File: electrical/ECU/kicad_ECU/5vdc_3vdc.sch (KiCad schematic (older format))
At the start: 8 parts

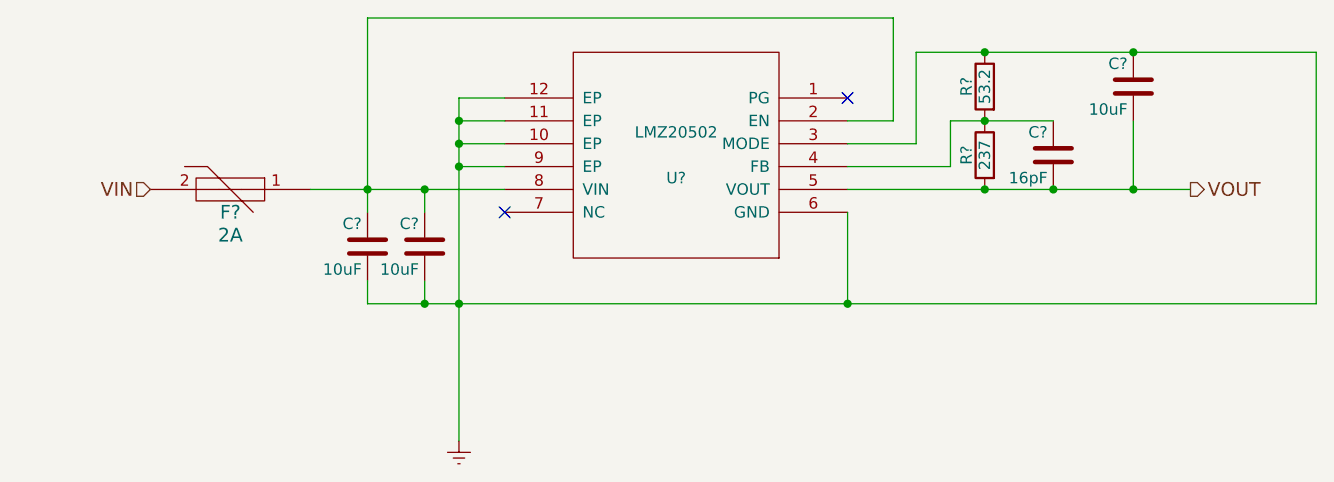
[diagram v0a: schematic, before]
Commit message: fixed some naming errors and initial round of double checking
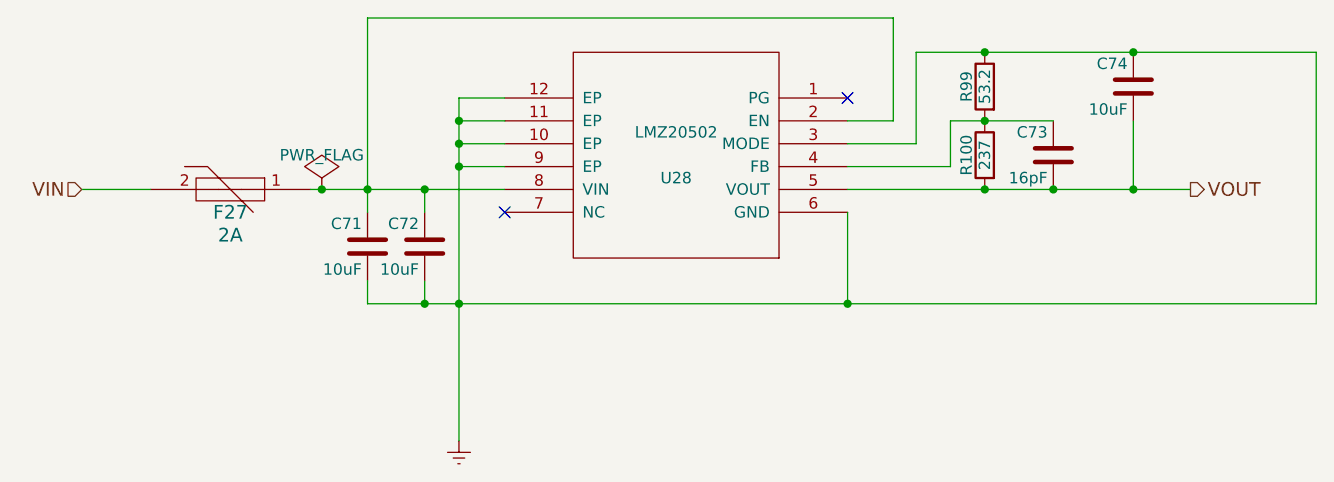
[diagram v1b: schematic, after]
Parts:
- gave numbers to parts that had none: 8
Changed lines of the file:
@@
 $Descr A4 11693 8268
 encoding utf-8
-Sheet 6 33
+Sheet 30 33
 Title "LMZ20502 5v to 3.3v"
 Date ""
@@
 $EndDescr
 $Comp
-L LMZ20502 U?
+L LMZ20502 U8
 U 1 1 59718A46
 P 5350 3350
-AR Path="/5978A36B/5978B8AA/59718A46" Ref="U?"  Part="1"
-AR Path="/597003E2/597189AE/59718A46" Ref="U?"  Part="1"
-F 0 "U?" H 5350 3250 50  0000 C CNN
+AR Path="/597003E2/597189AE/59718A46" Ref="U8"  Part="1"
+AR Path="/5978A36B/5978B8AA/59718A46" Ref="U28"  Part="1"
+F 0 "U28" H 5350 3250 50  0000 C CNN
 F 1 "LMZ20502" H 5350 3450 50  0000 C CNN
 F 2 "MODULE" H 5350 3350 50  0001 C CNN
@@
 	-1   0    0    -1
 $EndComp
-Text HLabel 3050 3500 0    60   Input ~ 0
+Text HLabel 2750 3500 0    60   Input ~ 0
 VIN
 NoConn ~ 4600 3600
@@
 NoConn ~ 6100 3100
 $Comp
-L Earth #PWR?
+L Earth #PWR22
 U 1 1 59718C19
 P 4400 4600
-AR Path="/5978A36B/5978B8AA/59718C19" Ref="#PWR?"  Part="1"
-AR Path="/597003E2/597189AE/59718C19" Ref="#PWR?"  Part="1"
-F 0 "#PWR?" H 4400 4350 50  0001 C CNN
+AR Path="/597003E2/597189AE/59718C19" Ref="#PWR22"  Part="1"
+AR Path="/5978A36B/5978B8AA/59718C19" Ref="#PWR67"  Part="1"
+F 0 "#PWR67" H 4400 4350 50  0001 C CNN
 F 1 "Earth" H 4400 4450 50  0001 C CNN
 F 2 "" H 4400 4600 50  0001 C CNN
@@
 $EndComp
 $Comp
-L C C?
+L C C23
 U 1 1 59718C97
 P 4250 3750
-AR Path="/5978A36B/5978B8AA/59718C97" Ref="C?"  Part="1"
-AR Path="/597003E2/597189AE/59718C97" Ref="C?"  Part="1"
-F 0 "C?" H 4275 3850 50  0000 L CNN
+AR Path="/597003E2/597189AE/59718C97" Ref="C23"  Part="1"
+AR Path="/5978A36B/5978B8AA/59718C97" Ref="C72"  Part="1"
+F 0 "C72" H 4275 3850 50  0000 L CNN
 F 1 "10uF" H 4275 3650 50  0000 L CNN
 F 2 "" H 4288 3600 50  0001 C CNN
@@
 $EndComp
 $Comp
-L C C?
+L C C22
 U 1 1 59718CB8
 P 4000 3750
-AR Path="/5978A36B/5978B8AA/59718CB8" Ref="C?"  Part="1"
-AR Path="/597003E2/597189AE/59718CB8" Ref="C?"  Part="1"
-F 0 "C?" H 4025 3850 50  0000 L CNN
+AR Path="/597003E2/597189AE/59718CB8" Ref="C22"  Part="1"
+AR Path="/5978A36B/5978B8AA/59718CB8" Ref="C71"  Part="1"
+F 0 "C71" H 4025 3850 50  0000 L CNN
 F 1 "10uF" H 4025 3650 50  0000 L CNN
 F 2 "" H 4038 3600 50  0001 C CNN
@@
 $EndComp
 $Comp
-L C C?
+L C C24
 U 1 1 59718DA5
 P 7000 3350
-AR Path="/5978A36B/5978B8AA/59718DA5" Ref="C?"  Part="1"
-AR Path="/597003E2/597189AE/59718DA5" Ref="C?"  Part="1"
-F 0 "C?" H 7025 3450 50  0000 L CNN
+AR Path="/597003E2/597189AE/59718DA5" Ref="C24"  Part="1"
+AR Path="/5978A36B/5978B8AA/59718DA5" Ref="C73"  Part="1"
+F 0 "C73" H 7025 3450 50  0000 L CNN
 F 1 "16pF" H 7025 3250 50  0000 L CNN
 F 2 "" H 7038 3200 50  0001 C CNN
@@
 $EndComp
 $Comp
-L R R?
+L R R23
 U 1 1 59718E45
 P 6700 3050
-AR Path="/5978A36B/5978B8AA/59718E45" Ref="R?"  Part="1"
-AR Path="/597003E2/597189AE/59718E45" Ref="R?"  Part="1"
-F 0 "R?" V 6780 3050 50  0000 C CNN
+AR Path="/597003E2/597189AE/59718E45" Ref="R23"  Part="1"
+AR Path="/5978A36B/5978B8AA/59718E45" Ref="R99"  Part="1"
+F 0 "R99" V 6780 3050 50  0000 C CNN
 F 1 "53.2" V 6700 3050 50  0000 C CNN
 F 2 "" V 6630 3050 50  0001 C CNN
@@
 $EndComp
 $Comp
-L R R?
+L R R24
 U 1 1 59718E7C
 P 6700 3350
-AR Path="/5978A36B/5978B8AA/59718E7C" Ref="R?"  Part="1"
-AR Path="/597003E2/597189AE/59718E7C" Ref="R?"  Part="1"
-F 0 "R?" V 6780 3350 50  0000 C CNN
+AR Path="/597003E2/597189AE/59718E7C" Ref="R24"  Part="1"
+AR Path="/5978A36B/5978B8AA/59718E7C" Ref="R100"  Part="1"
+F 0 "R100" V 6780 3350 50  0000 C CNN
 F 1 "237" V 6700 3350 50  0000 C CNN
 F 2 "" V 6630 3350 50  0001 C CNN
@@
 $EndComp
 $Comp
-L C C?
+L C C25
 U 1 1 59718FB7
 P 7350 3050
-AR Path="/5978A36B/5978B8AA/59718FB7" Ref="C?"  Part="1"
-AR Path="/597003E2/597189AE/59718FB7" Ref="C?"  Part="1"
-F 0 "C?" H 7375 3150 50  0000 L CNN
+AR Path="/597003E2/597189AE/59718FB7" Ref="C25"  Part="1"
+AR Path="/5978A36B/5978B8AA/59718FB7" Ref="C74"  Part="1"
+F 0 "C74" H 7375 3150 50  0000 L CNN
 F 1 "10uF" H 7375 2950 50  0000 L CNN
 F 2 "" H 7388 2900 50  0001 C CNN
@@
 Connection ~ 7350 2900
 $Comp
-L PTC_FUSE F?
+L PTC_FUSE F2
 U 1 1 5973811D
 P 3400 3500
-AR Path="/5978A36B/5978B8AA/5973811D" Ref="F?"  Part="1"
-AR Path="/597003E2/597189AE/5973811D" Ref="F?"  Part="1"
-F 0 "F?" H 3400 3400 60  0000 C CNN
+AR Path="/597003E2/597189AE/5973811D" Ref="F2"  Part="1"
+AR Path="/5978A36B/5978B8AA/5973811D" Ref="F27"  Part="1"
+F 0 "F27" H 3400 3400 60  0000 C CNN
 F 1 "2A" H 3400 3300 60  0000 C CNN
 F 2 "" H 3400 3500 60  0000 C CNN
@@
 	-1   0    0    -1
 $EndComp
+Wire Wire Line
+	2750 3500 3050 3500
+$Comp
+L PWR_FLAG #FLG10
+U 1 1 599195CA
+P 3800 3500
+AR Path="/597003E2/597189AE/599195CA" Ref="#FLG10"  Part="1"
+AR Path="/5978A36B/5978B8AA/599195CA" Ref="#FLG12"  Part="1"
+F 0 "#FLG12" H 3800 3575 50  0001 C CNN
+F 1 "PWR_FLAG" H 3800 3650 50  0000 C CNN
+F 2 "" H 3800 3500 50  0001 C CNN
+F 3 "" H 3800 3500 50  0001 C CNN
+	1    3800 3500
+	1    0    0    -1
+$EndComp
+Connection ~ 3800 3500
 $EndSCHEMATC
